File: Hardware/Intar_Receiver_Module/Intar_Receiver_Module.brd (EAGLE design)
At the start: 17.8 x 25.9 mm, 11 parts, among them J1 GROVE-4P-2.0-3470130P1, SW1 SWITCH_MOMENTARY

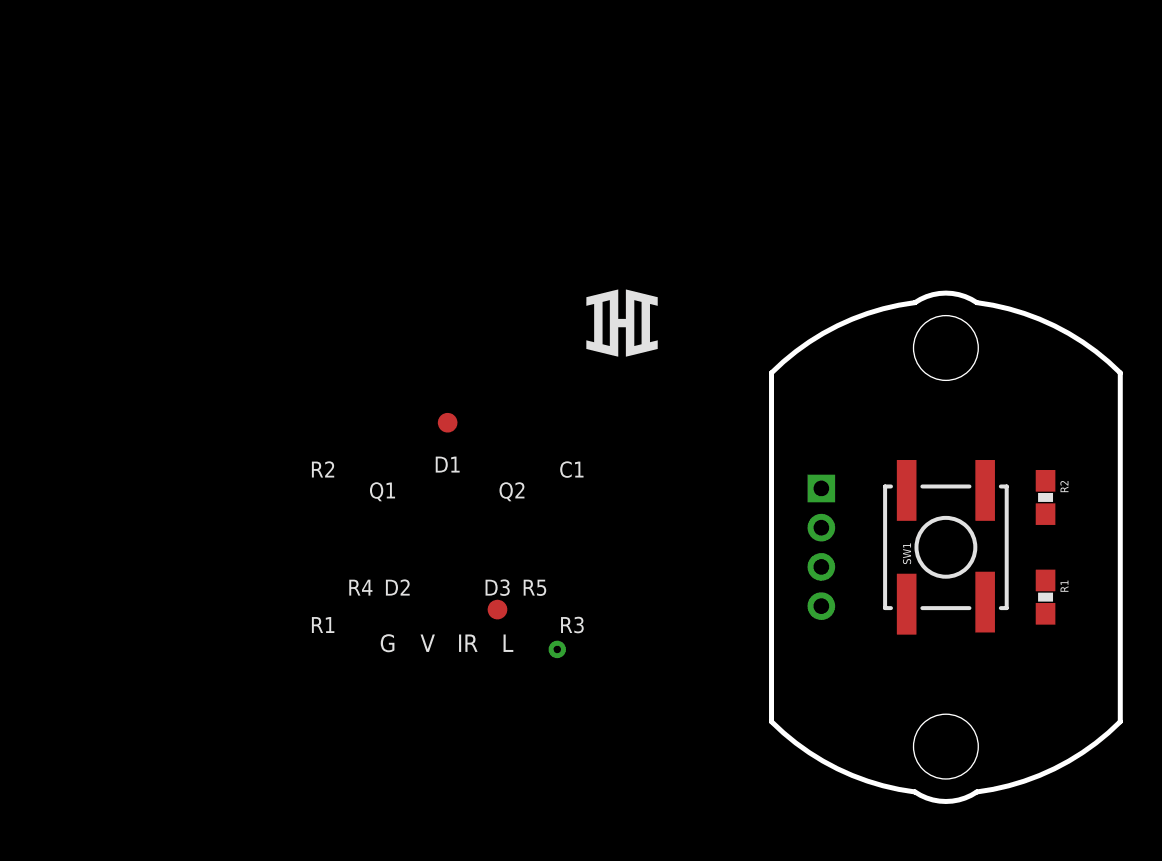
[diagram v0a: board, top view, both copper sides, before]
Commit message: Created schematics for first round of modules.
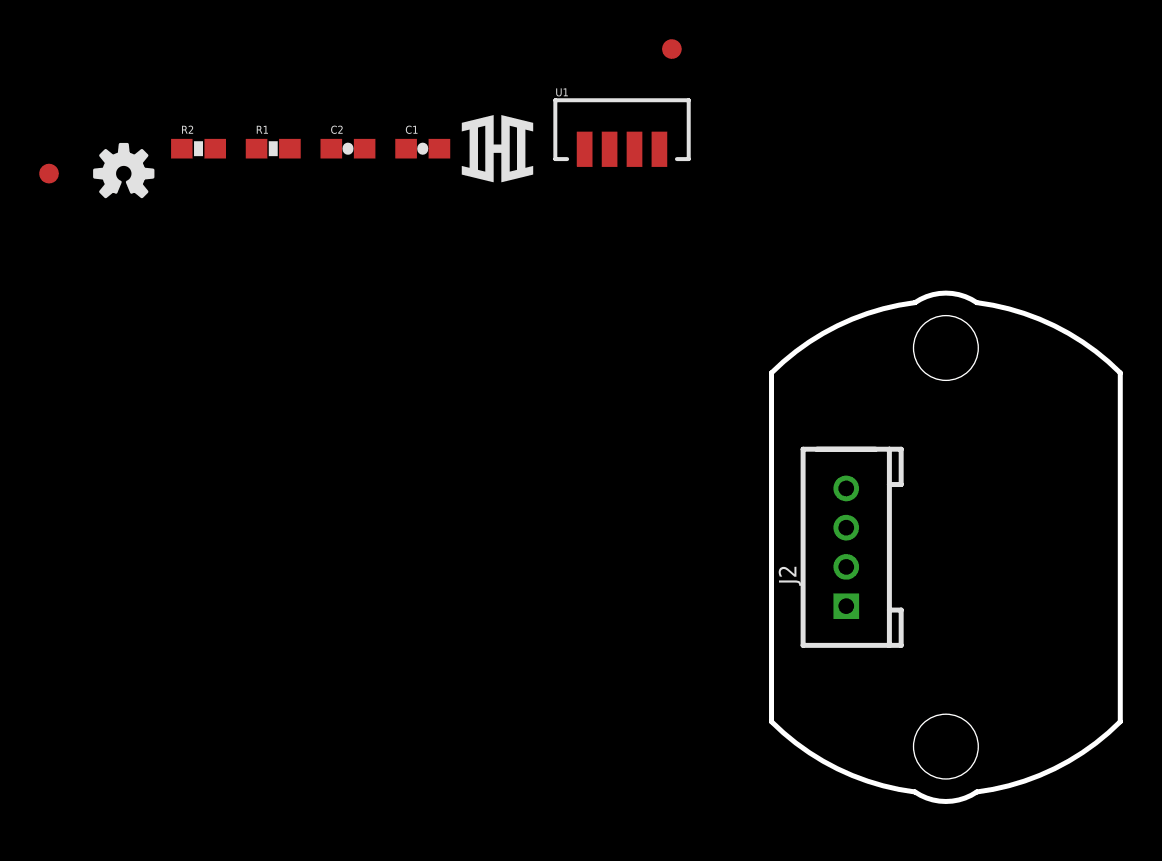
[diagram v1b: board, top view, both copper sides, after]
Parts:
- removed J1: GROVE-4P-2.0-3470130P1, Connector:4P-2.0
- removed SW1: SWITCH_MOMENTARY, Intar_Eagle_Library:KSCXXXG
- added C1: 1.0uF, SparkFun-Capacitors:0603-CAP
- added C2: 47nF, SparkFun-Capacitors:0603-CAP
- added J2: GROVE-4P-2.0-3470130P1, Connector:4P-2.0
- added U1: IR_RECEIVER, Intar_Eagle_Library:TSOP754XXW
- R1: value 10K -> 100
- R2: value 100 -> 2.2k
- moved FRAME1 72.7 mm to (-101.6, 1.27)
- moved R2 46.7 mm to (-38.1, 20.3), turned to 0 degrees
- moved R1 45.5 mm to (-34.3, 20.3), turned to 0 degrees
- moved FID2 29.9 mm to (-14.0, 25.4)
- moved FID1 24.0 mm to (-45.7, 19.1)
- moved LOGO1 23.8 mm to (-41.9, 19.1), flipped to the top
- moved U$1 10.9 mm to (-22.9, 20.3)
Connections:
- removed net BTN: J1.1, R2.1
- removed net N$1: R1.1, R2.2, SW1.1, SW1.2
- new net N$2: C1.1, R1.1, U1.2
- new net OUT: C2.1, R2.1, U1.3
- new net RX: J2.4
- net GND: now also C1.2, C2.2, J2.1, U1.1, U1.4; no longer J1.4, SW1.3, SW1.4
- net VCC: now also J2.2, R2.2; no longer J1.3
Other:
- board text removed: "C1"
- board text removed: "D1"
- board text removed: "D2"
- board text removed: "D3"
- board text removed: "G"
- board text removed: "IR"
- board text removed: "Intar IR LED Module"
- board text removed: "L"
- board text removed: "Q1"
- board text removed: "Q2"
- board text removed: "R1"
- board text removed: "R2"
- board text removed: "R3"
- board text removed: "R4"
- board text removed: "R5"
- board text removed: "Shawn Hymel"
- board text removed: "V"
- board text removed: "Visible LEDs"
- board text removed: "v01"

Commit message: Arranged components on all modules
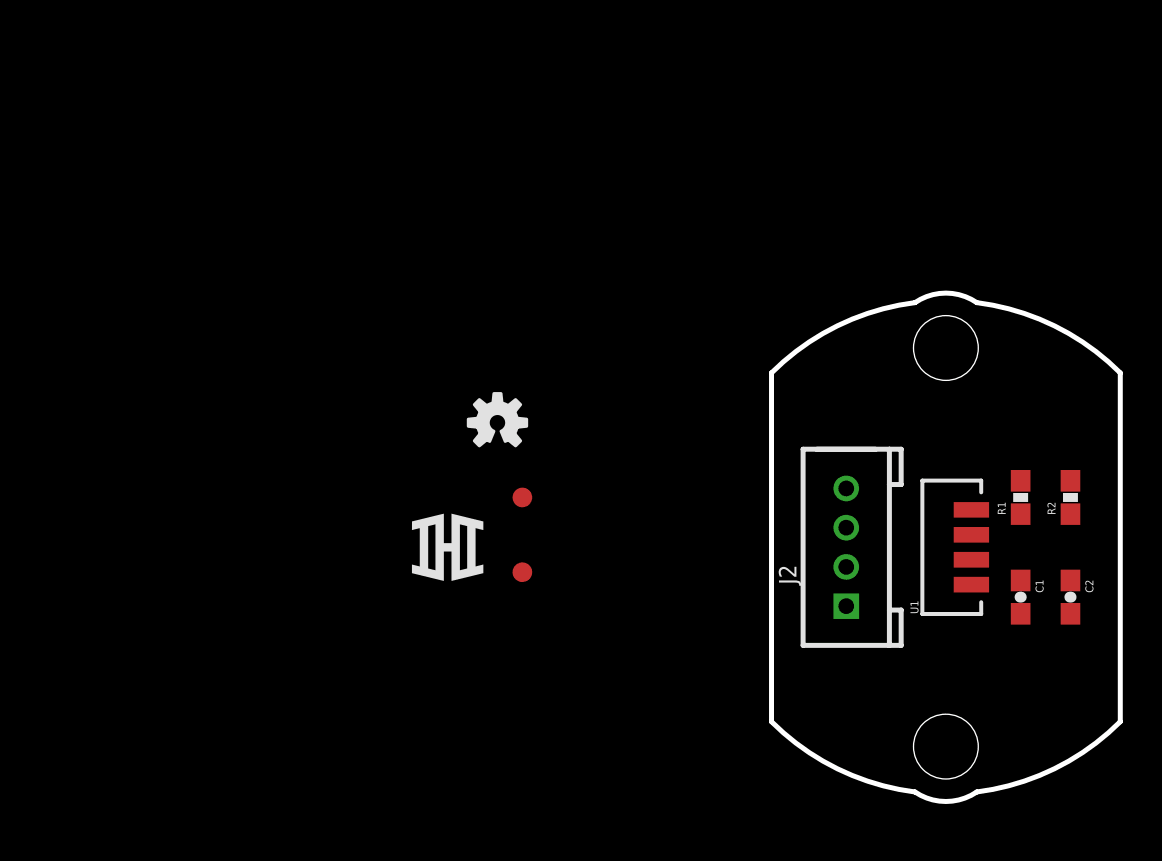
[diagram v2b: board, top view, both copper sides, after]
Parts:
- moved FRAME1 77.5 mm to (-27.9, -22.9)
- moved R2 47.9 mm to (6.35, 2.54), turned to 90 degrees
- moved C2 43.3 mm to (6.35, -2.54), turned to 270 degrees
- moved R1 42.0 mm to (3.81, 2.54), turned to 90 degrees
- moved C1 38.1 mm to (3.81, -2.54), turned to 270 degrees
- moved FID1 29.2 mm to (-21.6, 2.54)
- moved FID2 27.7 mm to (-21.6, -1.27)
- moved U1 27.2 mm to (0.00, 0.00), turned to 90 degrees
- moved LOGO1 22.9 mm to (-22.9, 6.35)
- moved U$1 20.5 mm to (-25.4, 0.00)
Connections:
- removed net RX: J2.4
- net OUT: now also J2.4
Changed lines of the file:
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@@
 <setting verticaltext="up"/>
 </settings>
-<grid distance="0.05" unitdist="inch" unit="inch" style="dots" multiple="1" display="yes" altdistance="0.005" altunitdist="inch" altunit="inch"/>
+<grid distance="0.05" unitdist="inch" unit="inch" style="dots" multiple="1" display="yes" altdistance="0.025" altunitdist="inch" altunit="inch"/>
 <layers>
 <layer number="1" name="Top" color="4" fill="1" visible="yes" active="yes"/>
 <layer number="2" name="Route2" color="1" fill="3" visible="no" active="yes"/>
 <layer number="15" name="Route15" color="4" fill="6" visible="no" active="yes"/>
-<layer number="16" name="Bottom" color="1" fill="1" visible="yes" active="yes"/>
+<layer number="16" name="Bottom" color="1" fill="1" visible="no" active="yes"/>
 <layer number="17" name="Pads" color="2" fill="1" visible="yes" active="yes"/>
 <layer number="18" name="Vias" color="2" fill="1" visible="yes" active="yes"/>
@@
 <layer number="20" name="Dimension" color="15" fill="1" visible="yes" active="yes"/>
 <layer number="21" name="tPlace" color="16" fill="1" visible="yes" active="yes"/>
-<layer number="22" name="bPlace" color="14" fill="1" visible="yes" active="yes"/>
+<layer number="22" name="bPlace" color="14" fill="1" visible="no" active="yes"/>
 <layer number="23" name="tOrigins" color="15" fill="1" visible="yes" active="yes"/>
-<layer number="24" name="bOrigins" color="15" fill="1" visible="yes" active="yes"/>
+<layer number="24" name="bOrigins" color="15" fill="1" visible="no" active="yes"/>
 <layer number="25" name="tNames" color="7" fill="1" visible="no" active="yes"/>
 <layer number="26" name="bNames" color="7" fill="1" visible="no" active="yes"/>
@@
 <layer number="43" name="vRestrict" color="2" fill="10" visible="no" active="yes"/>
 <layer number="44" name="Drills" color="7" fill="1" visible="no" active="yes"/>
-<layer number="45" name="Holes" color="7" fill="1" visible="yes" active="yes"/>
+<layer number="45" name="Holes" color="7" fill="1" visible="no" active="yes"/>
 <layer number="46" name="Milling" color="3" fill="1" visible="no" active="yes"/>
 <layer number="47" name="Measures" color="7" fill="1" visible="no" active="yes"/>
-<layer number="51" name="tDocu" color="6" fill="1" visible="yes" active="yes"/>
+<layer number="51" name="tDocu" color="6" fill="1" visible="no" active="yes"/>
 <layer number="52" name="bDocu" color="7" fill="1" visible="no" active="yes"/>
 <layer number="3" name="Route3" color="4" fill="3" visible="no" active="no"/>
@@
 </autorouter>
 <elements>
-<element name="C1" library="SparkFun-Capacitors" package="0603-CAP" value="1.0uF" x="-26.67" y="20.32">
-<attribute name="PROD_ID" value="CAP-00868" x="-26.67" y="20.32" size="1.778" layer="27" display="off"/>
+<element name="C1" library="SparkFun-Capacitors" package="0603-CAP" value="1.0uF" x="3.81" y="-2.54" rot="R270">
+<attribute name="PROD_ID" value="CAP-00868" x="3.81" y="-2.54" size="1.778" layer="27" rot="R270" display="off"/>
 </element>
-<element name="C2" library="SparkFun-Capacitors" package="0603-CAP" value="47nF" x="-30.48" y="20.32">
-<attribute name="PROD_ID" value="CAP-08605" x="-30.48" y="20.32" size="1.778" layer="27" display="off"/>
+<element name="C2" library="SparkFun-Capacitors" package="0603-CAP" value="47nF" x="6.35" y="-2.54" rot="R270">
+<attribute name="PROD_ID" value="CAP-08605" x="6.35" y="-2.54" size="1.778" layer="27" rot="R270" display="off"/>
 </element>
-<element name="FID1" library="SparkFun-Aesthetics" package="FIDUCIAL-1X2" value="FIDUCIAL1X2" x="-45.72" y="19.05"/>
-<element name="FID2" library="SparkFun-Aesthetics" package="FIDUCIAL-1X2" value="FIDUCIAL1X2" x="-13.97" y="25.4"/>
-<element name="FRAME1" library="SparkFun-Aesthetics" package="CREATIVE_COMMONS" value="FRAME-LETTER" x="-101.6" y="1.27"/>
+<element name="FID1" library="SparkFun-Aesthetics" package="FIDUCIAL-1X2" value="FIDUCIAL1X2" x="-21.59" y="2.54"/>
+<element name="FID2" library="SparkFun-Aesthetics" package="FIDUCIAL-1X2" value="FIDUCIAL1X2" x="-21.59" y="-1.27"/>
+<element name="FRAME1" library="SparkFun-Aesthetics" package="CREATIVE_COMMONS" value="FRAME-LETTER" x="-27.94" y="-22.86"/>
 <element name="J2" library="Connector" package="4P-2.0" value="GROVE-4P-2.0-3470130P1" x="-5.08" y="0" rot="R90"/>
-<element name="LOGO1" library="SparkFun-Aesthetics" package="OSHW-LOGO-S" value="OSHW-LOGOS" x="-41.91" y="19.05"/>
-<element name="R1" library="SparkFun-Resistors" package="0603-RES" value="100" x="-34.29" y="20.32">
-<attribute name="PROD_ID" value="RES-07863" x="-34.29" y="20.32" size="1.778" layer="27" display="off"/>
+<element name="LOGO1" library="SparkFun-Aesthetics" package="OSHW-LOGO-S" value="OSHW-LOGOS" x="-22.86" y="6.35"/>
+<element name="R1" library="SparkFun-Resistors" package="0603-RES" value="100" x="3.81" y="2.54" rot="R90">
+<attribute name="PROD_ID" value="RES-07863" x="3.81" y="2.54" size="1.778" layer="27" rot="R90" display="off"/>
 </element>
-<element name="R2" library="SparkFun-Resistors" package="0603-RES" value="2.2k" x="-38.1" y="20.32">
-<attribute name="PROD_ID" value="RES-08272" x="-38.1" y="20.32" size="1.778" layer="27" display="off"/>
+<element name="R2" library="SparkFun-Resistors" package="0603-RES" value="2.2k" x="6.35" y="2.54" rot="R90">
+<attribute name="PROD_ID" value="RES-08272" x="6.35" y="2.54" size="1.778" layer="27" rot="R90" display="off"/>
 </element>
 <element name="STANDOFF1" library="SparkFun-Electromechanical" package="STAND-OFF" value="STAND-OFF" x="0" y="-10.16"/>
 <element name="STANDOFF2" library="SparkFun-Electromechanical" package="STAND-OFF" value="STAND-OFF" x="0" y="10.16"/>
-<element name="U$1" library="Intar_Eagle_Library" package="LOGO_SM" value="LOGOSM" x="-22.86" y="20.32"/>
-<element name="U1" library="Intar_Eagle_Library" package="TSOP754XXW" value="IR_RECEIVER" x="-16.51" y="21.59"/>
+<element name="U$1" library="Intar_Eagle_Library" package="LOGO_SM" value="LOGOSM" x="-25.4" y="0"/>
+<element name="U1" library="Intar_Eagle_Library" package="TSOP754XXW" value="IR_RECEIVER" x="0" y="0" rot="R90"/>
 </elements>
 <signals>
-<signal name="GND">
+<signal name="GND" airwireshidden="yes">
 <contactref element="J2" pad="1"/>
 <contactref element="U1" pad="1"/>
@@
 <contactref element="C1" pad="2"/>
 <contactref element="C2" pad="2"/>
-<wire x1="-25.82" y1="20.32" x2="-5.08" y2="-3" width="0" layer="19" extent="1-1"/>
-<wire x1="-29.63" y1="20.32" x2="-25.82" y2="20.32" width="0" layer="19" extent="1-1"/>
-<wire x1="-18.415" y1="20.29" x2="-25.82" y2="20.32" width="0" layer="19" extent="1-1"/>
-<wire x1="-14.605" y1="20.29" x2="-18.415" y2="20.29" width="0" layer="19" extent="1-1"/>
+<wire x1="1.3" y1="-1.905" x2="-5.08" y2="-3" width="0" layer="19" extent="1-1"/>
+<wire x1="3.81" y1="-3.39" x2="1.3" y2="-1.905" width="0" layer="19" extent="1-1"/>
+<wire x1="6.35" y1="-3.39" x2="3.81" y2="-3.39" width="0" layer="19" extent="1-1"/>
+<wire x1="1.3" y1="1.905" x2="1.3" y2="-1.905" width="0" layer="19" extent="1-1"/>
 </signal>
 <signal name="VCC">
@@
 <contactref element="R1" pad="2"/>
 <contactref element="R2" pad="2"/>
-<wire x1="-33.44" y1="20.32" x2="-37.25" y2="20.32" width="0" layer="19" extent="1-1"/>
-<wire x1="-5.08" y1="-1" x2="-33.44" y2="20.32" width="0" layer="19" extent="1-1"/>
-</signal>
-<signal name="RX">
-<contactref element="J2" pad="4"/>
+<wire x1="3.81" y1="3.39" x2="6.35" y2="3.39" width="0" layer="19" extent="1-1"/>
+<wire x1="-5.08" y1="-1" x2="3.81" y2="3.39" width="0" layer="19" extent="1-1"/>
 </signal>
 <signal name="N$2">
@@
 <contactref element="C1" pad="1"/>
 <contactref element="R1" pad="1"/>
-<wire x1="-27.52" y1="20.32" x2="-35.14" y2="20.32" width="0" layer="19" extent="1-1"/>
-<wire x1="-17.145" y1="20.29" x2="-27.52" y2="20.32" width="0" layer="19" extent="1-1"/>
+<wire x1="1.3" y1="-0.635" x2="3.81" y2="-1.69" width="0" layer="19" extent="1-1"/>
+<wire x1="3.81" y1="1.69" x2="3.81" y2="-1.69" width="0" layer="19" extent="1-1"/>
 </signal>
 <signal name="OUT">
@@
 <contactref element="R2" pad="1"/>
 <contactref element="C2" pad="1"/>
-<wire x1="-31.33" y1="20.32" x2="-38.95" y2="20.32" width="0" layer="19" extent="1-1"/>
-<wire x1="-15.875" y1="20.29" x2="-31.33" y2="20.32" width="0" layer="19" extent="1-1"/>
+<contactref element="J2" pad="4"/>
+<wire x1="6.35" y1="-1.69" x2="6.35" y2="1.69" width="0" layer="19" extent="1-1"/>
+<wire x1="1.3" y1="0.635" x2="6.35" y2="1.69" width="0" layer="19" extent="1-1"/>
+<wire x1="-5.08" y1="3" x2="1.3" y2="0.635" width="0" layer="19" extent="1-1"/>
 </signal>
 </signals>

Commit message: Fixed Grove connectors to be right way (pin 4 should be GND)
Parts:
- removed J2: GROVE-4P-2.0-3470130P1, Connector:4P-2.0
- added J1: GROVE-4P-2.0-3470130P1, Connector:4P-2.0
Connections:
- net GND: now also J1.4; no longer J2.1
- net OUT: now also J1.1; no longer J2.4
- net VCC: now also J1.3; no longer J2.2
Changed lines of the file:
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@@
 <setting verticaltext="up"/>
 </settings>
-<grid distance="0.05" unitdist="inch" unit="inch" style="dots" multiple="1" display="yes" altdistance="0.025" altunitdist="inch" altunit="inch"/>
+<grid distance="0.05" unitdist="inch" unit="inch" style="dots" multiple="1" display="yes" altdistance="0.005" altunitdist="inch" altunit="inch"/>
 <layers>
 <layer number="1" name="Top" color="4" fill="1" visible="yes" active="yes"/>
 <layer number="2" name="Route2" color="1" fill="3" visible="no" active="yes"/>
 <layer number="15" name="Route15" color="4" fill="6" visible="no" active="yes"/>
-<layer number="16" name="Bottom" color="1" fill="1" visible="no" active="yes"/>
+<layer number="16" name="Bottom" color="1" fill="1" visible="yes" active="yes"/>
 <layer number="17" name="Pads" color="2" fill="1" visible="yes" active="yes"/>
 <layer number="18" name="Vias" color="2" fill="1" visible="yes" active="yes"/>
@@
 <layer number="20" name="Dimension" color="15" fill="1" visible="yes" active="yes"/>
 <layer number="21" name="tPlace" color="16" fill="1" visible="yes" active="yes"/>
-<layer number="22" name="bPlace" color="14" fill="1" visible="no" active="yes"/>
+<layer number="22" name="bPlace" color="14" fill="1" visible="yes" active="yes"/>
 <layer number="23" name="tOrigins" color="15" fill="1" visible="yes" active="yes"/>
-<layer number="24" name="bOrigins" color="15" fill="1" visible="no" active="yes"/>
+<layer number="24" name="bOrigins" color="15" fill="1" visible="yes" active="yes"/>
 <layer number="25" name="tNames" color="7" fill="1" visible="no" active="yes"/>
 <layer number="26" name="bNames" color="7" fill="1" visible="no" active="yes"/>
@@
 <layer number="43" name="vRestrict" color="2" fill="10" visible="no" active="yes"/>
 <layer number="44" name="Drills" color="7" fill="1" visible="no" active="yes"/>
-<layer number="45" name="Holes" color="7" fill="1" visible="no" active="yes"/>
+<layer number="45" name="Holes" color="7" fill="1" visible="yes" active="yes"/>
 <layer number="46" name="Milling" color="3" fill="1" visible="no" active="yes"/>
 <layer number="47" name="Measures" color="7" fill="1" visible="no" active="yes"/>
-<layer number="51" name="tDocu" color="6" fill="1" visible="no" active="yes"/>
+<layer number="51" name="tDocu" color="6" fill="1" visible="yes" active="yes"/>
 <layer number="52" name="bDocu" color="7" fill="1" visible="no" active="yes"/>
 <layer number="3" name="Route3" color="4" fill="3" visible="no" active="no"/>
@@
 <element name="FID2" library="SparkFun-Aesthetics" package="FIDUCIAL-1X2" value="FIDUCIAL1X2" x="-21.59" y="-1.27"/>
 <element name="FRAME1" library="SparkFun-Aesthetics" package="CREATIVE_COMMONS" value="FRAME-LETTER" x="-27.94" y="-22.86"/>
-<element name="J2" library="Connector" package="4P-2.0" value="GROVE-4P-2.0-3470130P1" x="-5.08" y="0" rot="R90"/>
 <element name="LOGO1" library="SparkFun-Aesthetics" package="OSHW-LOGO-S" value="OSHW-LOGOS" x="-22.86" y="6.35"/>
 <element name="R1" library="SparkFun-Resistors" package="0603-RES" value="100" x="3.81" y="2.54" rot="R90">
@@
 <element name="U$1" library="Intar_Eagle_Library" package="LOGO_SM" value="LOGOSM" x="-25.4" y="0"/>
 <element name="U1" library="Intar_Eagle_Library" package="TSOP754XXW" value="IR_RECEIVER" x="0" y="0" rot="R90"/>
+<element name="J1" library="Connector" package="4P-2.0" value="GROVE-4P-2.0-3470130P1" x="-19.05" y="-7.62" rot="MR270"/>
 </elements>
 <signals>
 <signal name="GND" airwireshidden="yes">
-<contactref element="J2" pad="1"/>
 <contactref element="U1" pad="1"/>
 <contactref element="U1" pad="4"/>
 <contactref element="C1" pad="2"/>
 <contactref element="C2" pad="2"/>
-<wire x1="1.3" y1="-1.905" x2="-5.08" y2="-3" width="0" layer="19" extent="1-1"/>
+<contactref element="J1" pad="4"/>
+<wire x1="1.3" y1="-1.905" x2="-19.05" y2="-10.62" width="0" layer="19" extent="1-1"/>
 <wire x1="3.81" y1="-3.39" x2="1.3" y2="-1.905" width="0" layer="19" extent="1-1"/>
 <wire x1="6.35" y1="-3.39" x2="3.81" y2="-3.39" width="0" layer="19" extent="1-1"/>
@@
 </signal>
 <signal name="VCC">
-<contactref element="J2" pad="2"/>
 <contactref element="R1" pad="2"/>
 <contactref element="R2" pad="2"/>
-<wire x1="3.81" y1="3.39" x2="6.35" y2="3.39" width="0" layer="19" extent="1-1"/>
-<wire x1="-5.08" y1="-1" x2="3.81" y2="3.39" width="0" layer="19" extent="1-1"/>
+<contactref element="J1" pad="3"/>
+<wire x1="3.81" y1="3.39" x2="-19.05" y2="-8.62" width="0" layer="19" extent="1-1"/>
+<wire x1="6.35" y1="3.39" x2="3.81" y2="3.39" width="0" layer="19" extent="1-1"/>
 </signal>
 <signal name="N$2">
@@
 <contactref element="R2" pad="1"/>
 <contactref element="C2" pad="1"/>
-<contactref element="J2" pad="4"/>
+<contactref element="J1" pad="1"/>
+<wire x1="1.3" y1="0.635" x2="-19.05" y2="-4.62" width="0" layer="19" extent="1-1"/>
+<wire x1="6.35" y1="1.69" x2="1.3" y2="0.635" width="0" layer="19" extent="1-1"/>
 <wire x1="6.35" y1="-1.69" x2="6.35" y2="1.69" width="0" layer="19" extent="1-1"/>
-<wire x1="1.3" y1="0.635" x2="6.35" y2="1.69" width="0" layer="19" extent="1-1"/>
-<wire x1="-5.08" y1="3" x2="1.3" y2="0.635" width="0" layer="19" extent="1-1"/>
 </signal>
 </signals>
